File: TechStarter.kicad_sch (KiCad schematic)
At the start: 32 parts, among them J1 Conn_01x04_Socket, J10 Conn_01x03_Socket, J11 Conn_01x03_Socket, J12 Conn_01x04_Pin, J2 Conn_01x04_Socket, J3 Conn_01x02_Socket, J4 Conn_01x04_Socket, J5 Conn_01x03_Socket, J6 Conn_01x04_Socket, J7 Conn_01x03_Socket, J8 Conn_01x03_Socket, J9 Conn_01x03_Socket, Q1 SI2312, U1 STM32F446RETx, U2 TMC2209-LA, U3 TMC2209-LA, U5 MX25L3233FM1

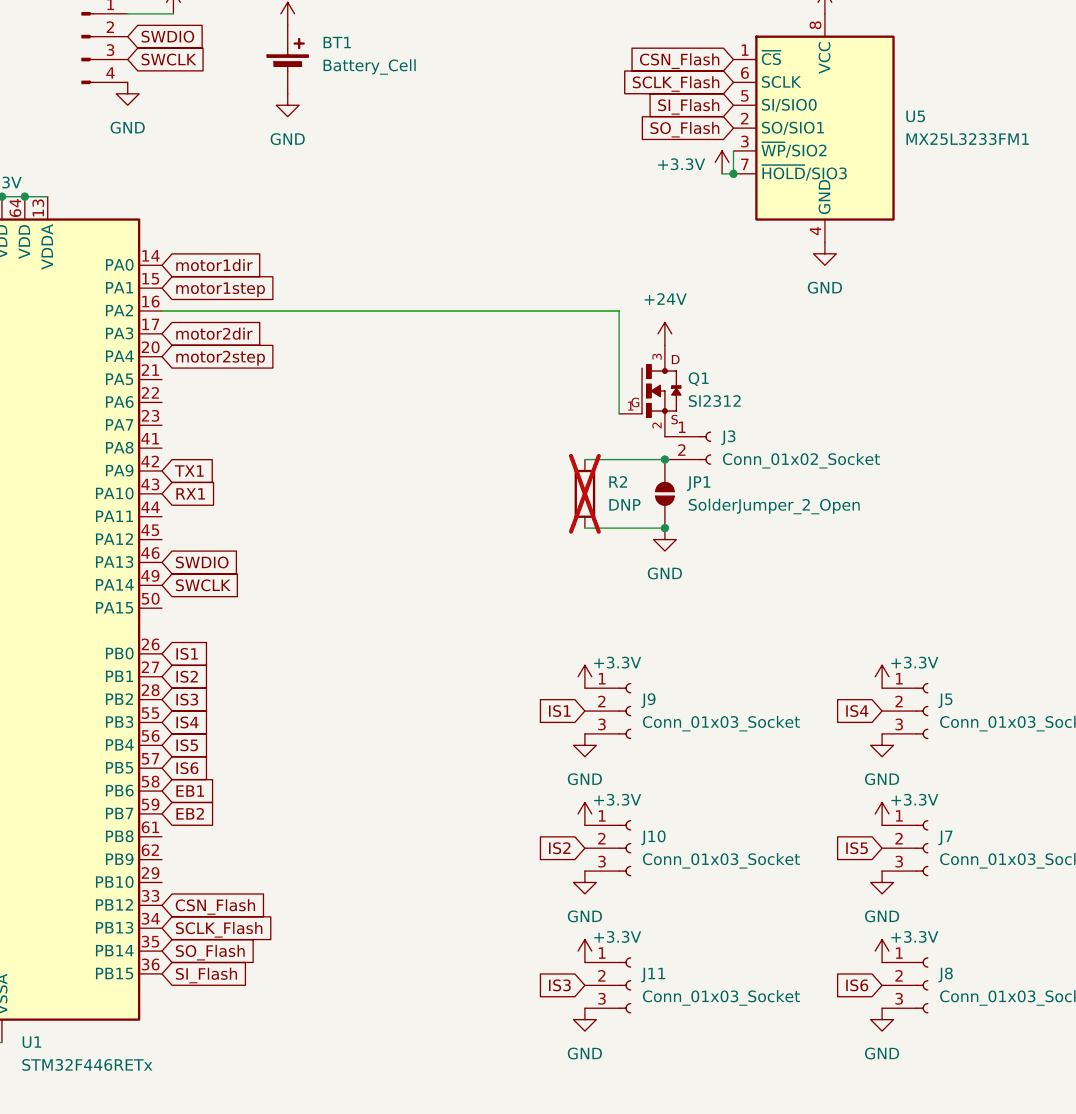
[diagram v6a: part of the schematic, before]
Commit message: Values and finishing touches
I ve seen you put bad values for capacitors in powerbrick and added the value of the feedback resistor, also I redid the inductor circuit because gemini said so and your mosfet was for 20 V not 24 V ...
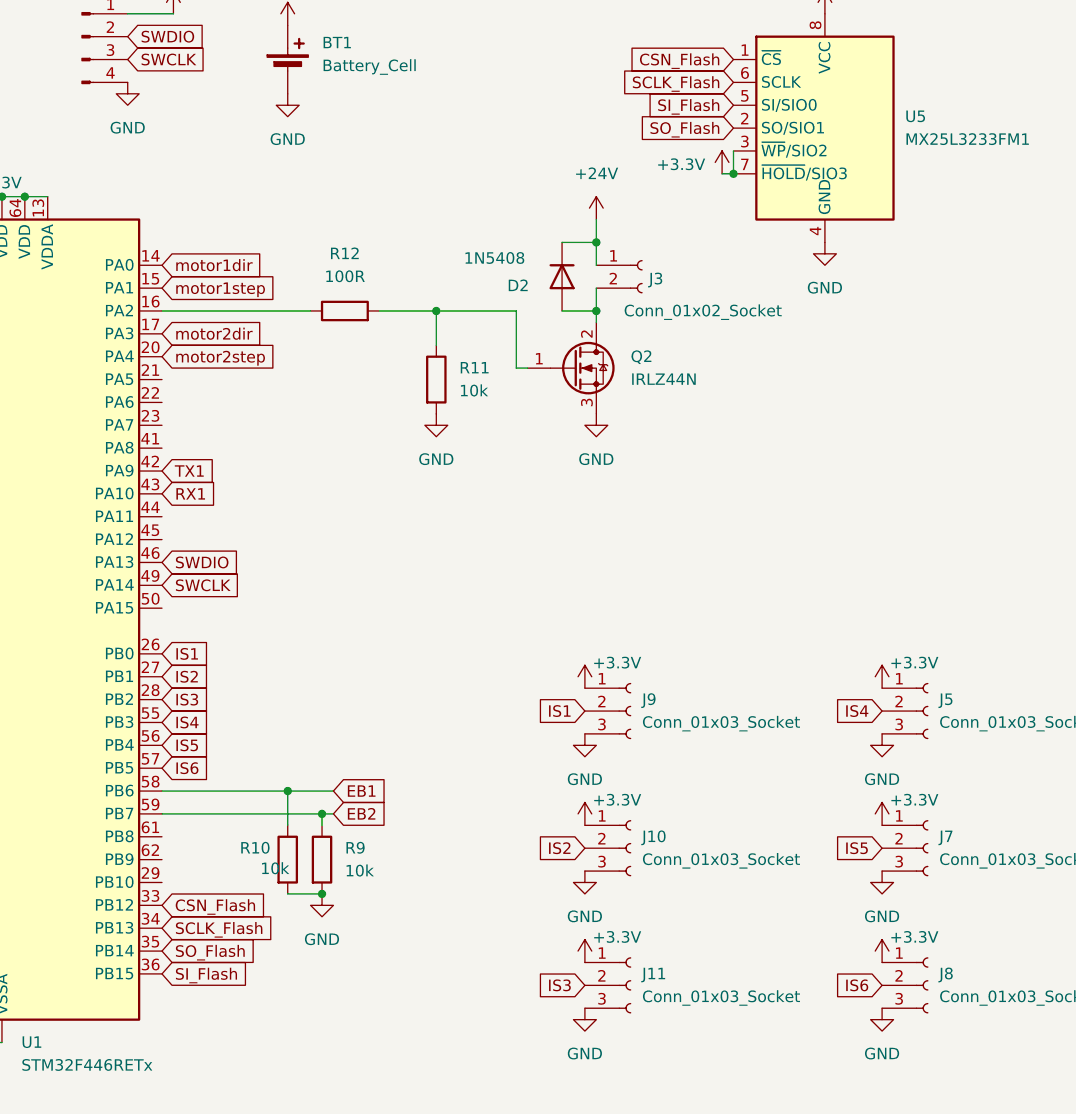
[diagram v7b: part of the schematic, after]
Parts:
- removed JP1: SolderJumper_2_Open, symbol Jumper:SolderJumper_2_Open
- removed Q1: SI2312, SI2312:SOT23, symbol SI2312:SI2312
- removed R2: DNP, symbol Device:R
- added D2: 1N5408, Diode_THT:D_DO-201AD_P15.24mm_Horizontal, symbol Diode:1N5408
- added Q2: IRLZ44N, Package_TO_SOT_THT:TO-220-3_Vertical, symbol Transistor_FET:IRLZ44N
- added R10, R11, R9: 10k, symbol Device:R
- added R12: 100R, symbol Device:R
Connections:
- net +24V: now also J3.1 (Pin_1), D2.1 (K)
- net EB1: now also R10.1
- net EB2: now also R9.1
- net GND: now also Q2.3 (S), R10.2, R11.2, R9.2
- net at J3.2 (Pin_2): now also D2.2 (A), Q2.2 (D)
- net at U1.16 (PA2): now also R12.1
- new net: Q2.1 (G), R11.1, R12.2
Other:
- moved on the sheet: J3

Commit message: .
označení sekcí
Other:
- note added: "Display"
- note added: "End buttons"
- note added: "Induction sensors"
- note added: "Inductor for pneumatic rotaty thing"
- note added: "Programmer"
- moved on the sheet: J10, J11, J4, J5, J6, J7, J8, J9, U5
